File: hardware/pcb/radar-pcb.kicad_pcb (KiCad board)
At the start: 2 copper layers, 66 x 128 mm, 55 parts, among them J1 USB-C zasilanie 5 V (GCT USB4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, J2 DevKit J1, J3 DevKit J3, J4 HC-SR04 (kabel): VCC TRIG ECH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, J5 Serwo SG90 (kabel): GND +5V S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, J6 MAX7219 Elegoo: VCC GND DIN C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, J7 OLED SH1106: VCC GND SCK SDA, J8 Buzzer: + -, J9 Przycisk zewnetrzny, Q2 MMBT3904, SW1 Przycisk ON/standby (katowy), U1 SN74AHCT125N

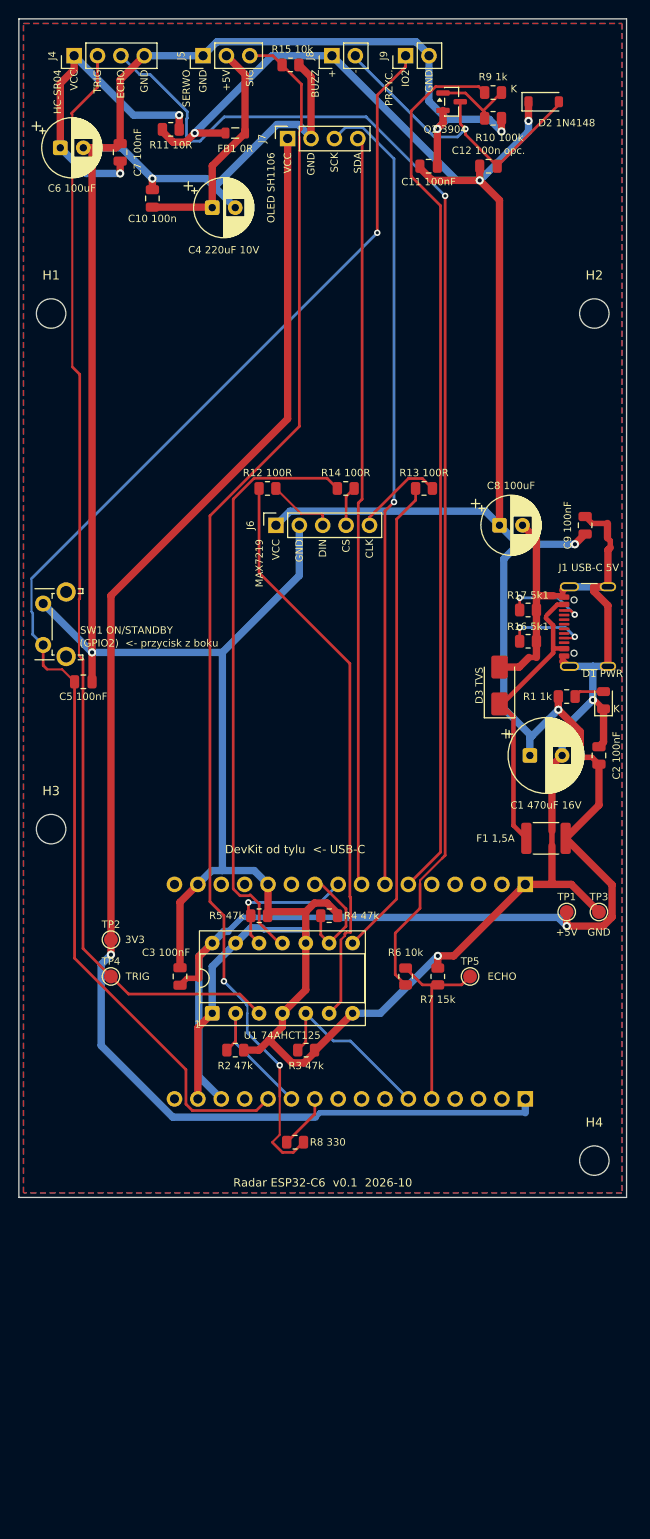
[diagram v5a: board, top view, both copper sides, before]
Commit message: PCB: apply audit findings (load switch, D4, SOIC buffer, CS pull-up, antenna keepout, ADC sense), clean silkscreen
Co-Authored-By: Claude Sonnet 5.5 <noreply@anthropic.com>
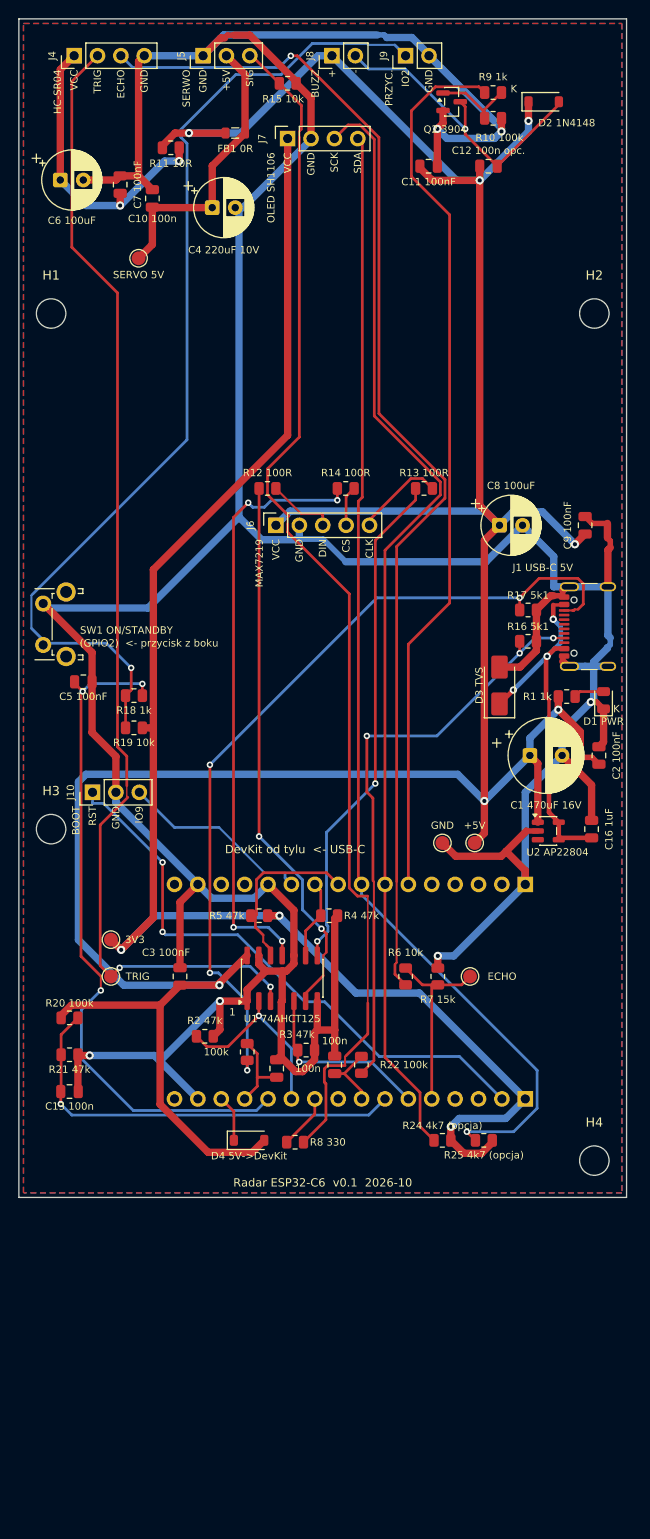
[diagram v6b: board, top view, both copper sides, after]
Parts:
- removed F1: Polyfuse 1,5 A, Fuse:Fuse_1812_4532Metric
- added C13: 100 nF, Capacitor_SMD:C_0805_2012Metric, F.Cu at (105.5, 141.5)
- added C14: 100 nF, Capacitor_SMD:C_0805_2012Metric, F.Cu at (134.3, 138.6)
- added C15: 100 nF, Capacitor_SMD:C_0805_2012Metric, F.Cu at (128.0, 139.0)
- added C16: 1 uF, Capacitor_SMD:C_0805_2012Metric, F.Cu at (162.2, 113.0)
- added D4: 1N5819HW, Diode_SMD:D_SOD-123, F.Cu at (125.0, 146.8)
- added J10: Awaryjne wgrywanie: RST GND BOOT (zwarcie sasiednich), Connector_PinHeader_2.54mm:PinHeader_1x03_P2.54mm_Vertical, F.Cu at (108.0, 109.0)
- added R18: 1 k, Resistor_SMD:R_0805_2012Metric, F.Cu at (112.5, 98.5)
- added R19: 10 k, Resistor_SMD:R_0805_2012Metric, F.Cu at (112.5, 102.0)
- added R20: 100 k, Resistor_SMD:R_0805_2012Metric, F.Cu at (105.5, 133.5)
- added R21: 47 k, Resistor_SMD:R_0805_2012Metric, F.Cu at (105.5, 137.5)
- added R22: 100 k, Resistor_SMD:R_0805_2012Metric, F.Cu at (137.2, 138.6)
- added R23: 100 k, Resistor_SMD:R_0805_2012Metric, F.Cu at (124.8, 137.2)
- added R24: 4,7 k (nie montowac), Resistor_SMD:R_0805_2012Metric, F.Cu at (146.0, 146.8)
- added R25: 4,7 k (nie montowac), Resistor_SMD:R_0805_2012Metric, F.Cu at (150.5, 146.8)
- added TP6: TP SERVO_5V, TestPoint:TestPoint_Pad_D1.5mm, F.Cu at (113.0, 51.0)
- added U2: AP22804AW5 (przelacznik 5 V, limit ok. 2,5-3 A), Package_TO_SOT_SMD:SOT-23-5, F.Cu at (157.5, 113.2)
- D3: value SMAJ5.0CA (TVS 5 V) -> SMAJ5.0A (TVS 5 V, jednokierunkowy)
- FB1: value Ferryt >=1 A lub 0 R -> 0 R (zworka; opcja: ferryt >= 1 A)
- U1: value SN74AHCT125N -> SN74AHCT125D; footprint Package_DIP:DIP-14_W7.62mm_Socket -> Package_SO:SOIC-14_3.9x8.7mm_P1.27mm
- moved TP3 18.6 mm to (146.0, 114.5)
- moved TP1 12.5 mm to (149.5, 114.5)
- moved U1 8.50 mm to (128.6, 129.2)
- moved R2 3.62 mm to (120.2, 135.5)
- moved C6 3.50 mm to (104.5, 42.5)
- moved C7 3.50 mm to (111.0, 43.0)
- moved R15 2.02 mm to (129.2, 32.0)
- moved R11 2.00 mm to (116.5, 39.0)
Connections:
- C5 pad 1: BTN -> BTN_ESP
- J2 pad 12: BTN -> BTN_ESP
- J2 pad 13: unconnected-(J2-Pin_13-Pad13) -> CC2_SENSE
- J2 pad 14: +5V -> DEVKIT_5V
- J2 pad 2: unconnected-(J2-Pin_2-Pad2) -> EN
- J2 pad 7: unconnected-(J2-Pin_7-Pad7) -> V5_SENSE
- J2 pad 8: unconnected-(J2-Pin_8-Pad8) -> CC1_SENSE
- J3 pad 11: unconnected-(J3-Pin_11-Pad11) -> BOOT
- R5 pad 2: GND -> +3V3
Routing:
- net CC2: track 9.41 -> 91.6 mm, vias 2 -> 4
- net BTN_ESP: track 0.00 -> 74.4 mm, vias 0 -> 3
- net +5V: track 273.4 -> 338.2 mm, vias 6 -> 7
- net EN: track 0.00 -> 63.4 mm, vias 0 -> 2
- net CC1: track 9.13 -> 64.6 mm, vias 2 -> 3
- net V5_SENSE: track 0.00 -> 46.6 mm, vias 0 -> 1
- net SDA: track 81.5 -> 123.8 mm, vias 0 -> 1
- net BTN: track 148.3 -> 110.1 mm
- net GND: track 445.7 -> 482.4 mm
- net SCL: track 87.6 -> 122.0 mm, vias 1 -> 0
- net BOOT: track 0.00 -> 21.0 mm
- net +3V3: track 157.9 -> 170.0 mm, vias 1 -> 3
- net VIN: track 31.9 -> 41.4 mm, vias 0 -> 3
- net CC2_SENSE: track 0.00 -> 9.14 mm
- net CC1_SENSE: track 0.00 -> 7.20 mm
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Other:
- board text added: "100k"
- board text added: "100n"
- board text added: "BOOT"
- board text added: "C13 100n"
- board text added: "C16 1uF"
- board text added: "D4 5V->DevKit"
- board text added: "R18 1k"
- board text added: "R19 10k"
- board text added: "R20 100k"
- board text added: "R21 47k"
- board text added: "R22 100k"
- board text added: "R24 4k7 (opcja)"
- board text added: "R25 4k7 (opcja)"
- board text added: "SERVO 5V"
- board text added: "U2 AP22804"
- board text removed: "F1 1,5A"

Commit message: PCB: second audit (U2 next to USB-C, J10 near RST/BOOT, FLG to GPIO23), docs and renders
Co-Authored-By: Claude Sonnet 5.5 <noreply@anthropic.com>
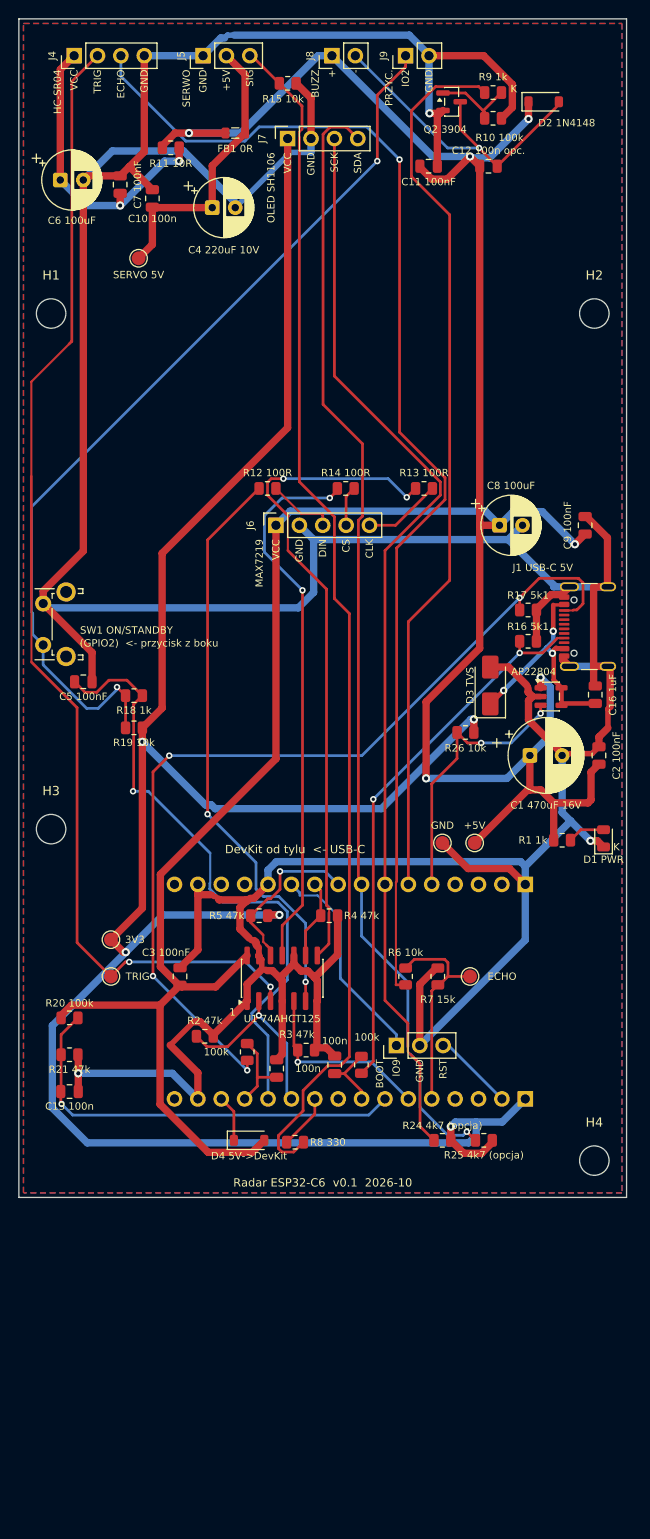
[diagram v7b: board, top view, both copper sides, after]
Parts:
- added R26: 10 k, Resistor_SMD:R_0805_2012Metric, F.Cu at (148.5, 102.5)
- J10: value Awaryjne wgrywanie: RST GND BOOT (zwarcie sasiednich) -> Awaryjne wgrywanie: BOOT GND RST (zworka na sasiednie piny)
- moved J10 43.0 mm to (141.0, 136.5)
- moved R1 15.6 mm to (159.0, 114.2)
- moved D1 15.0 mm to (163.5, 114.0)
- moved C16 14.6 mm to (162.6, 98.4)
- moved U2 14.6 mm to (157.8, 98.6)
- moved D3 1.00 mm to (151.2, 97.4)
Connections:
- J10 pad 1: EN -> BOOT
- J10 pad 3: BOOT -> EN
- J3 pad 5: unconnected-(J3-Pin_5-Pad5) -> U2_FLG
- U2 pad 3: unconnected-(U2-~{FLG}-Pad3) -> U2_FLG
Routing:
- net +3V3: track 170.0 -> 247.5 mm, vias 3 -> 5
- net EN: track 63.4 -> 8.78 mm, vias 2 -> 0
- net GND: track 482.4 -> 519.2 mm, vias 6 -> 3
- net U2_FLG: track 0.00 -> 29.4 mm, vias 0 -> 2
- net CLK_5V: track 55.3 -> 72.2 mm
- net VIN: track 41.4 -> 27.1 mm
- net BTN: track 110.1 -> 99.4 mm, vias 1 -> 2
- net +5V: track 338.2 -> 328.4 mm, vias 7 -> 6
- net CC2: track 91.6 -> 99.3 mm
- net BTN_ESP: track 74.4 -> 67.2 mm, vias 3 -> 1
- net CS_5V: track 65.7 -> 59.7 mm, vias 4 -> 2
- net CC1: track 64.6 -> 59.5 mm, vias 3 -> 2
- net DIN_5V: track 59.6 -> 63.4 mm
- net SCL: track 122.0 -> 118.3 mm
- net ECHO_3V3: track 20.5 -> 23.2 mm
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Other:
- board text added: "AP22804"
- board text added: "R26 10k"
- board text removed: "R22 100k"
- board text removed: "U2 AP22804"

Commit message: PCB: USB-C power jack and ON/STANDBY button on the left edge, measured DevKit and module dimensions, holes in a rectangle
Co-Authored-By: Claude Sonnet 5.5 <noreply@anthropic.com>
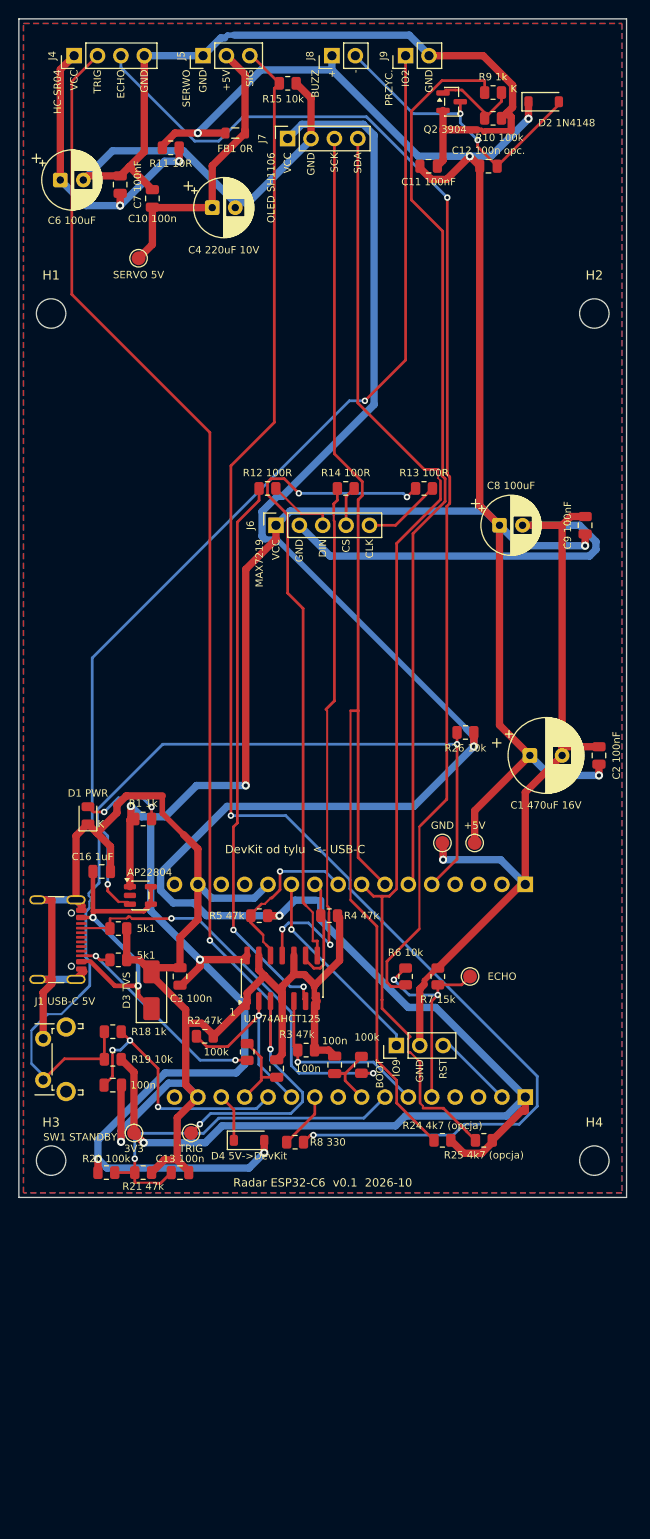
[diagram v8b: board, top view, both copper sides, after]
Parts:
- moved J1 68.8 mm to (103.1, 125.0), turned to -90 degrees
- moved R17 58.5 mm to (110.8, 127.2)
- moved C16 56.9 mm to (109.0, 117.6), turned to 0 degrees
- moved D1 56.1 mm to (107.5, 111.5)
- moved R16 54.3 mm to (110.8, 123.8)
- moved U2 49.6 mm to (113.2, 120.2)
- moved D3 49.5 mm to (114.4, 130.5)
- moved SW1 47.2 mm to (102.6, 140.2)
- moved R1 45.6 mm to (113.5, 111.9)
- moved C5 43.9 mm to (110.2, 140.8)
- moved R18 36.6 mm to (110.2, 135.0)
- moved R19 36.1 mm to (110.2, 138.0)
- moved H3 36.0 mm to (103.5, 149.0)
- moved TP2 21.1 mm to (112.5, 146.0)
- moved TP4 19.1 mm to (118.7, 146.0)
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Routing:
- net CC2: track 99.3 -> 24.4 mm, vias 4 -> 2
- net GND: track 519.2 -> 446.6 mm, vias 3 -> 2
- net BTN: track 99.4 -> 142.3 mm, vias 2 -> 1
- net U2_FLG: track 29.4 -> 71.9 mm
- net BTN_ESP: track 67.2 -> 28.9 mm, vias 1 -> 3
- net SERVO_SIG: track 130.8 -> 162.0 mm, vias 0 -> 2
- net TRIG_5V: track 127.2 -> 143.9 mm, vias 2 -> 3
- net SCL: track 118.3 -> 134.9 mm
- net CC1: track 59.5 -> 44.6 mm
- net VIN: track 27.1 -> 34.6 mm, vias 3 -> 2
- net +3V3: track 247.5 -> 254.3 mm, vias 5 -> 3
- net V5_SENSE: track 46.5 -> 40.4 mm
- net LED_A: track 4.06 -> 9.49 mm, vias 0 -> 2
- net BUZ_NEG: track 36.0 -> 32.4 mm, vias 1 -> 2
- net CLK_3V3: track 8.68 -> 12.1 mm
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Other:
- board text added: "5k1"
- board text added: "C3 100n"
- board text added: "SW1 STANDBY"
- board text added: "W10 DevKit: rozstaw rzedow pinow (srodek-srodek), ZMIERZONE 23,1 mm"
- board text added: "W11 DevKit: pin 1 - pin 16 jednej listwy (15 x 2,54 mm), ZMIERZONE 38,1 mm"
- board text added: "W12 DevKit: od prawej krawedzi (widok od frontu) do pinu 1, ZMIERZONE 11,0 mm"
- board text added: "W5 odstep gniazd OLED-MAX7219 (pion), ZMIERZONE 42,0 mm"
- board text added: "WYMIARY DO WERYFIKACJI (? = do potwierdzenia, OK = zmierzone lub zatwierdzone 2026-10-13)"
- board text removed: "(GPIO2) <- przycisk z boku"
- board text removed: "C3 100nF"
- board text removed: "C5 100nF"
- board text removed: "R16 5k1"
- board text removed: "R17 5k1"
- board text removed: "SW1 ON/STANDBY"
- board text removed: "W10 DevKit: rozstaw rzedow pinow (srodek-srodek), ZALOZONE 23,3 mm"
- board text removed: "W11 DevKit: pin 1 - pin 16 jednej listwy (15 x 2,54 mm)"
- board text removed: "W12 DevKit: od prawej krawedzi (widok od frontu) do pinu 1"
- board text removed: "W5 odstep gniazd OLED-MAX7219 (pion), zgodny z oknami w obudowie"
- board text removed: "WYMIARY DO WERYFIKACJI (? = wartosc z projektu)"
